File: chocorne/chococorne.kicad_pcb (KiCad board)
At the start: 2 copper layers, 130 x 87.7 mm, 59 parts, among them J1 MJ-4PP-9, J2 OLED, SW1 SW_PUSH, SW10 SW_PUSH, SW11 SW_PUSH, SW12 SW_PUSH, SW13 SW_PUSH, SW14 SW_PUSH, SW15 SW_PUSH, SW16 SW_PUSH, SW17 SW_PUSH, SW18 SW_PUSH, SW19 SW_PUSH, SW2 SW_PUSH, SW20 SW_PUSH, SW21 SW_PUSH, SW3 SW_PUSH, SW4 SW_PUSH, SW5 SW_PUSH, SW6 SW_PUSH, SW7 SW_PUSH, SW8 SW_PUSH, SW9 SW_PUSH, U1 ProMicro

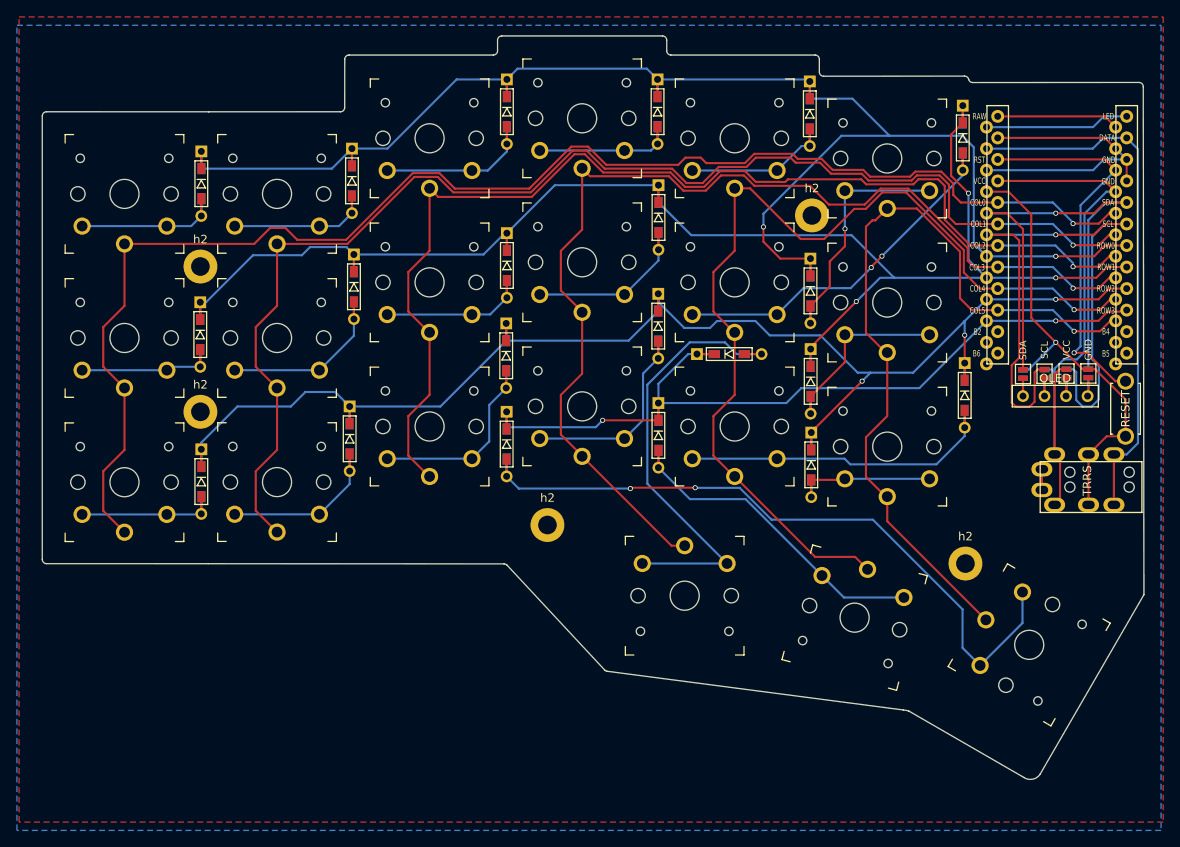
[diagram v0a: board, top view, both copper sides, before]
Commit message: old chocorne: update before deletion
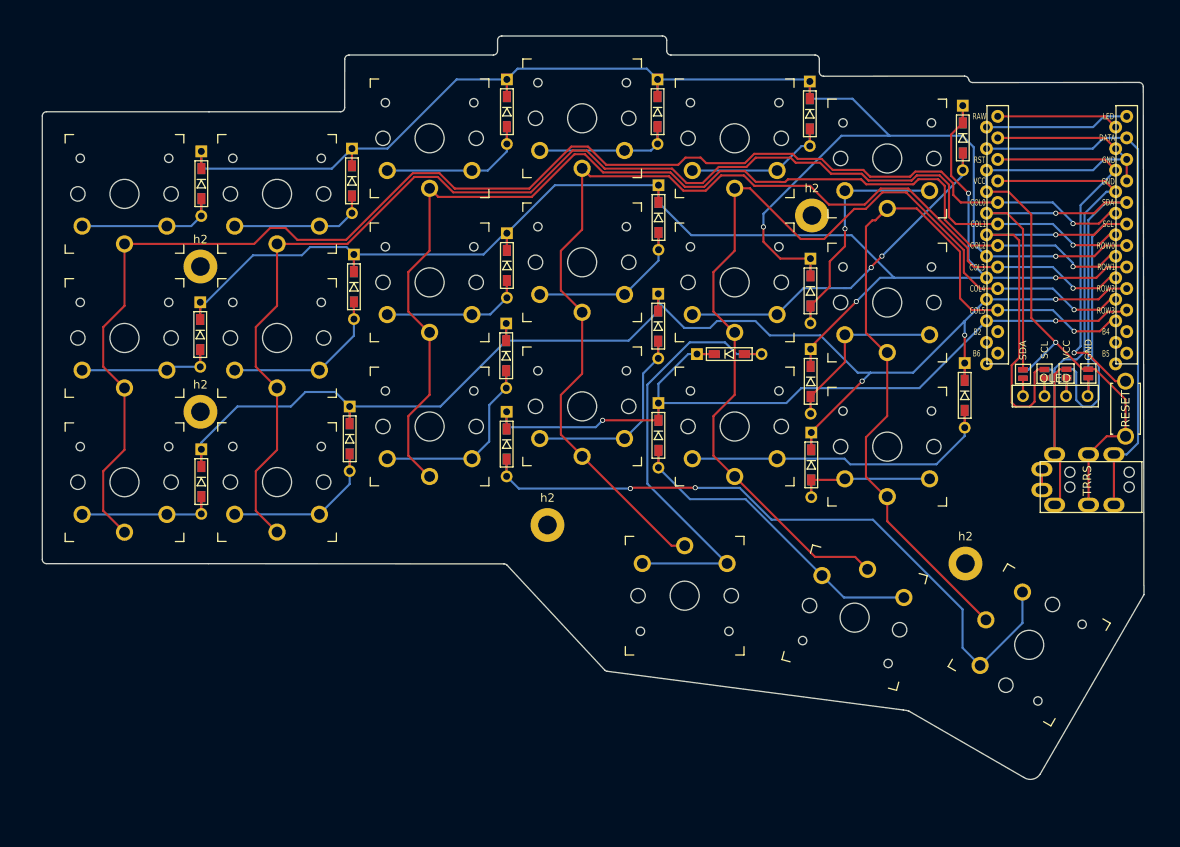
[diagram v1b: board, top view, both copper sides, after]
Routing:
- removed copper zone on B.Cu, net (none)
- removed copper zone on F.Cu, net (none)
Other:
- outline, holes or cut-outs redrawn
